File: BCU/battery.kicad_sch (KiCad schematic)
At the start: 5 parts

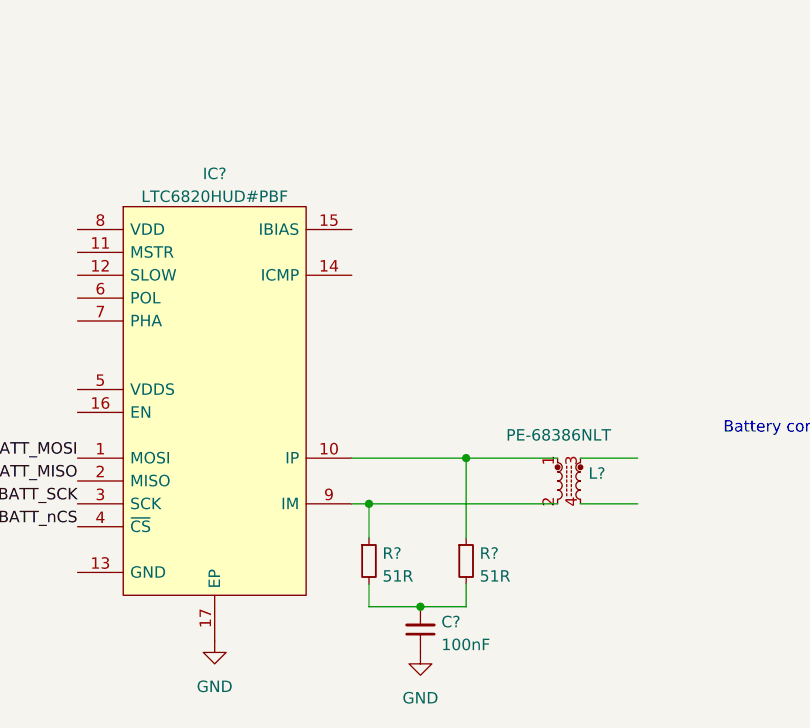
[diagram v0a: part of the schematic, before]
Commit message: Make rough component placement for evaluating missing 3D
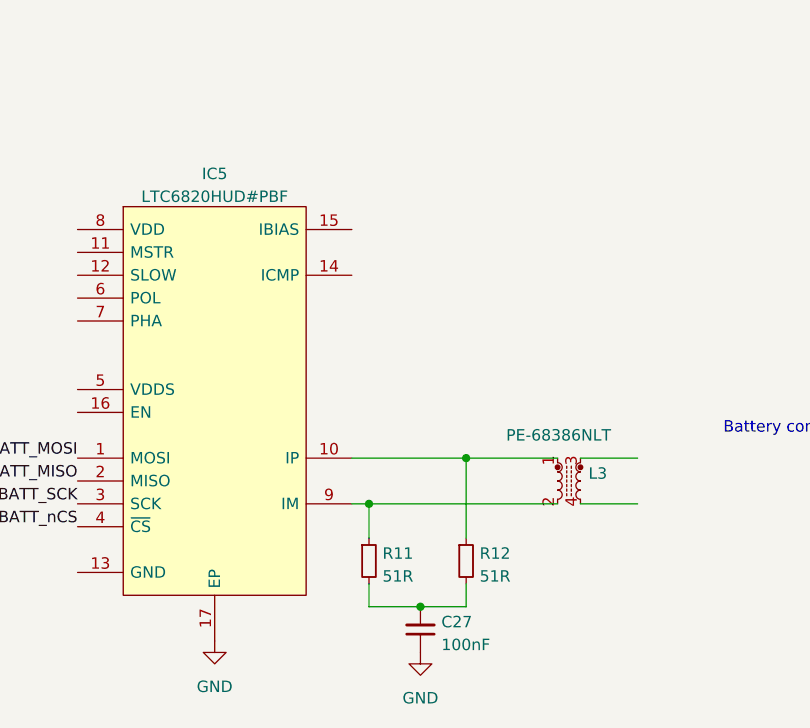
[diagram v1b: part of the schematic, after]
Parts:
- gave numbers to parts that had none: 5
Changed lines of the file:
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@@
   (symbol (lib_id "power:GND") (at 110.49 113.03 0) (unit 1)
     (in_bom yes) (on_board yes) (fields_autoplaced)
-    (property "Reference" "#PWR?" (id 0) (at 110.49 119.38 0)
+    (property "Reference" "#PWR0151" (id 0) (at 110.49 119.38 0)
       (effects (font (size 1.27 1.27)) hide)
     )
@@
   (symbol (lib_id "power:GND") (at 133.35 114.3 0) (unit 1)
     (in_bom yes) (on_board yes) (fields_autoplaced)
-    (property "Reference" "#PWR?" (id 0) (at 133.35 120.65 0)
+    (property "Reference" "#PWR0150" (id 0) (at 133.35 120.65 0)
       (effects (font (size 1.27 1.27)) hide)
     )
@@
   (symbol (lib_id "Device:R_Small") (at 138.43 104.14 0) (unit 1)
     (in_bom yes) (on_board yes) (fields_autoplaced)
-    (property "Reference" "R?" (id 0) (at 139.9286 103.3053 0)
+    (property "Reference" "R12" (id 0) (at 139.9286 103.3053 0)
       (effects (font (size 1.27 1.27)) (justify left))
     )
@@
   (symbol (lib_id "coilchain-com:LTC6820HUD#PBF") (at 110.49 64.77 0) (unit 1)
     (in_bom yes) (on_board yes) (fields_autoplaced)
-    (property "Reference" "IC?" (id 0) (at 110.49 61.121 0))
+    (property "Reference" "IC5" (id 0) (at 110.49 61.121 0))
     (property "Value" "LTC6820HUD#PBF" (id 1) (at 110.49 63.6579 0))
     (property "Footprint" "Package_DFN_QFN:QFN-16-1EP_3x3mm_P0.5mm_EP1.7x1.7mm" (id 2) (at 134.62 67.31 0)
@@
   (symbol (lib_id "Device:C_Small") (at 133.35 111.76 180) (unit 1)
     (in_bom yes) (on_board yes) (fields_autoplaced)
-    (property "Reference" "C?" (id 0) (at 135.6741 110.9189 0)
+    (property "Reference" "C27" (id 0) (at 135.6741 110.9189 0)
       (effects (font (size 1.27 1.27)) (justify right))
     )
@@
   (symbol (lib_id "Device:R_Small") (at 127.635 104.14 0) (unit 1)
     (in_bom yes) (on_board yes) (fields_autoplaced)
-    (property "Reference" "R?" (id 0) (at 129.1336 103.3053 0)
+    (property "Reference" "R11" (id 0) (at 129.1336 103.3053 0)
       (effects (font (size 1.27 1.27)) (justify left))
     )
@@
   (symbol (lib_id "Device:L_Ferrite_Coupled_Small") (at 149.86 95.25 90) (mirror x) (unit 1)
     (in_bom yes) (on_board yes)
-    (property "Reference" "L?" (id 0) (at 152.019 94.4153 90)
+    (property "Reference" "L3" (id 0) (at 152.019 94.4153 90)
       (effects (font (size 1.27 1.27)) (justify right))
     )

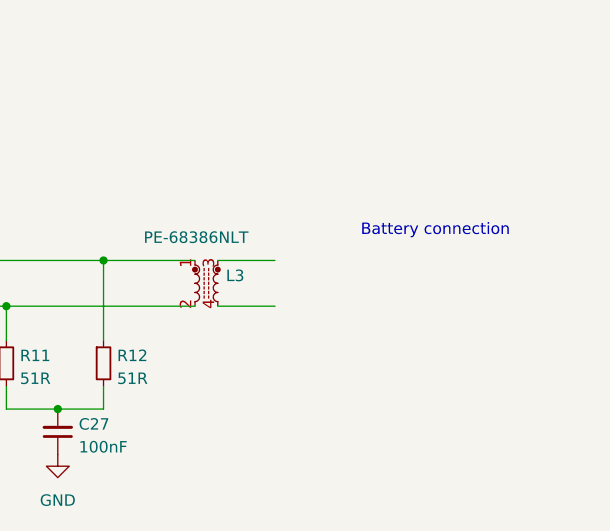
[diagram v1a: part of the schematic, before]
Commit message: change 48v to +BATT, increase cap sizes
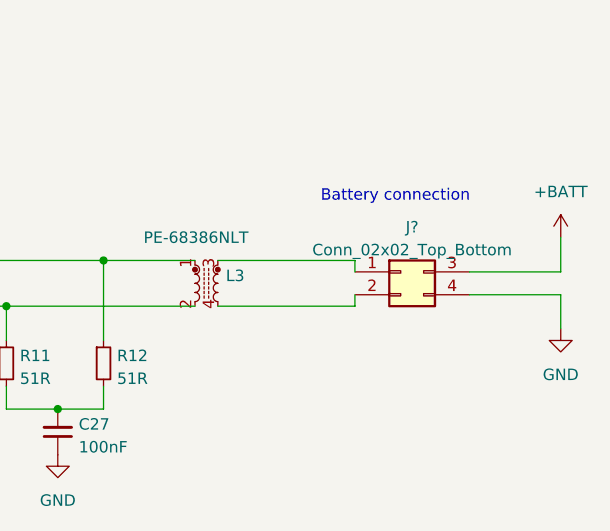
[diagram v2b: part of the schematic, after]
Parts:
- added J?: Conn_02x02_Top_Bottom, symbol Connector_Generic:Conn_02x02_Top_Bottom
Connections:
- net GND: now also J?.4 (Pin_4)
- net at L3.3: now also J?.1 (Pin_1)
- net at L3.4: now also J?.2 (Pin_2)
- new net +BATT: J?.3 (Pin_3)
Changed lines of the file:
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@@
+    (stroke (width 0) (type default) (color 0 0 0 0))
+  )
+  (wire (pts (xy 179.07 96.52) (xy 189.23 96.52))
+    (stroke (width 0) (type default) (color 0 0 0 0))
+  )
+  (wire (pts (xy 189.23 93.98) (xy 189.23 90.17))
     (stroke (width 0) (type default) (color 0 0 0 0))
   )
@@
     (stroke (width 0) (type default) (color 0 0 0 0))
   )
-  (wire (pts (xy 151.13 97.79) (xy 157.48 97.79))
+  (wire (pts (xy 166.37 92.71) (xy 166.37 93.98))
+    (stroke (width 0) (type default) (color 0 0 0 0))
+  )
+  (wire (pts (xy 151.13 97.79) (xy 166.37 97.79))
     (stroke (width 0) (type default) (color 0 0 0 0))
   )
@@
     (stroke (width 0) (type default) (color 0 0 0 0))
   )
+  (wire (pts (xy 179.07 93.98) (xy 189.23 93.98))
+    (stroke (width 0) (type default) (color 0 0 0 0))
+  )
   (wire (pts (xy 127.635 97.79) (xy 127.635 101.6))
     (stroke (width 0) (type default) (color 0 0 0 0))
@@
     (stroke (width 0) (type default) (color 0 0 0 0))
   )
+  (wire (pts (xy 189.23 96.52) (xy 189.23 100.33))
+    (stroke (width 0) (type default) (color 0 0 0 0))
+  )
   (wire (pts (xy 138.43 92.71) (xy 125.73 92.71))
     (stroke (width 0) (type default) (color 0 0 0 0))
@@
     (stroke (width 0) (type default) (color 0 0 0 0))
   )
-  (wire (pts (xy 151.13 92.71) (xy 157.48 92.71))
+  (wire (pts (xy 151.13 92.71) (xy 166.37 92.71))
     (stroke (width 0) (type default) (color 0 0 0 0))
   )
@@
     (stroke (width 0) (type default) (color 0 0 0 0))
   )
+  (wire (pts (xy 166.37 97.79) (xy 166.37 96.52))
+    (stroke (width 0) (type default) (color 0 0 0 0))
+  )
   (wire (pts (xy 36.83 24.13) (xy 46.99 24.13))
     (stroke (width 0) (type default) (color 0 0 0 0))
   )
-  (text "Battery connection" (at 167.005 90.17 0)
+  (text "Battery connection" (at 162.56 86.36 0)
     (effects (font (size 1.27 1.27)) (justify left bottom))
   )
@@
     (effects (font (size 1.27 1.27)) (justify right))
   )
+  (symbol (lib_id "power:+BATT") (at 189.23 90.17 0) (unit 1)
+    (in_bom yes) (on_board yes) (fields_autoplaced)
+    (property "Reference" "#PWR?" (id 0) (at 189.23 93.98 0)
+      (effects (font (size 1.27 1.27)) hide)
+    )
+    (property "Value" "+BATT" (id 1) (at 189.23 85.09 0))
+    (property "Footprint" "" (id 2) (at 189.23 90.17 0)
+      (effects (font (size 1.27 1.27)) hide)
+    )
+    (property "Datasheet" "" (id 3) (at 189.23 90.17 0)
+      (effects (font (size 1.27 1.27)) hide)
+    )
+    (pin "1")
+  )
   (symbol (lib_id "power:GND") (at 110.49 113.03 0) (unit 1)
     (in_bom yes) (on_board yes) (fields_autoplaced)
@@
     )
     (property "Datasheet" "" (id 3) (at 110.49 113.03 0)
+      (effects (font (size 1.27 1.27)) hide)
+    )
+    (pin "1")
+  )
+  (symbol (lib_id "power:GND") (at 189.23 100.33 0) (unit 1)
+    (in_bom yes) (on_board yes) (fields_autoplaced)
+    (property "Reference" "#PWR?" (id 0) (at 189.23 106.68 0)
+      (effects (font (size 1.27 1.27)) hide)
+    )
+    (property "Value" "GND" (id 1) (at 189.23 105.41 0))
+    (property "Footprint" "" (id 2) (at 189.23 100.33 0)
+      (effects (font (size 1.27 1.27)) hide)
+    )
+    (property "Datasheet" "" (id 3) (at 189.23 100.33 0)
       (effects (font (size 1.27 1.27)) hide)
     )
@@
     (pin "2")
   )
+  (symbol (lib_id "Connector_Generic:Conn_02x02_Top_Bottom") (at 171.45 93.98 0) (unit 1)
+    (in_bom yes) (on_board yes) (fields_autoplaced)
+    (property "Reference" "J?" (id 0) (at 172.72 89.0102 0))
+    (property "Value" "Conn_02x02_Top_Bottom" (id 1) (at 172.72 91.5471 0))
+    (property "Footprint" "" (id 2) (at 171.45 93.98 0)
+      (effects (font (size 1.27 1.27)) hide)
+    )
+    (property "Datasheet" "~" (id 3) (at 171.45 93.98 0)
+      (effects (font (size 1.27 1.27)) hide)
+    )
+    (pin "1")
+    (pin "2")
+    (pin "3")
+    (pin "4")
+  )
   (symbol (lib_id "Device:R_Small") (at 127.635 104.14 0) (unit 1)

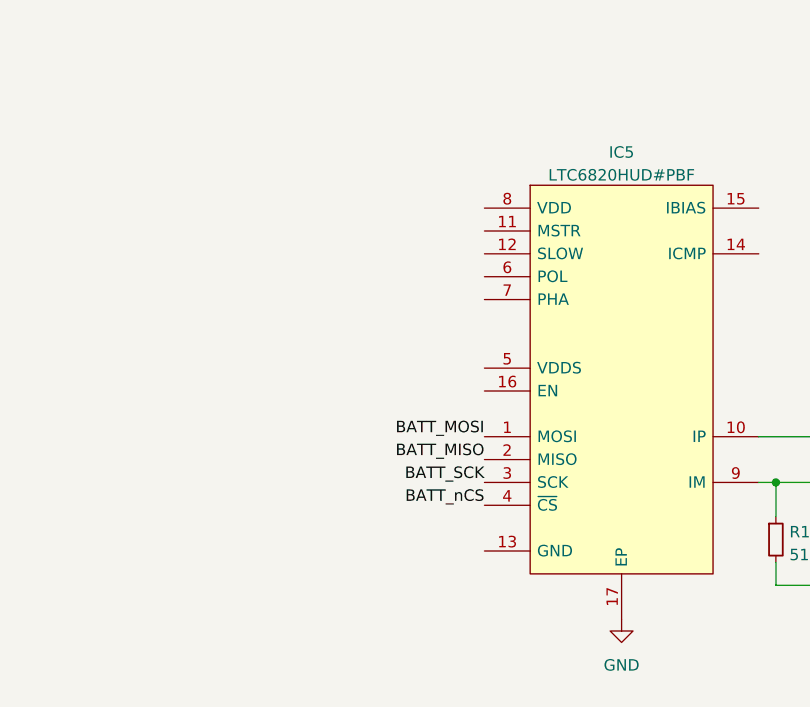
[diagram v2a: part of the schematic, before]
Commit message: Added power enable logic
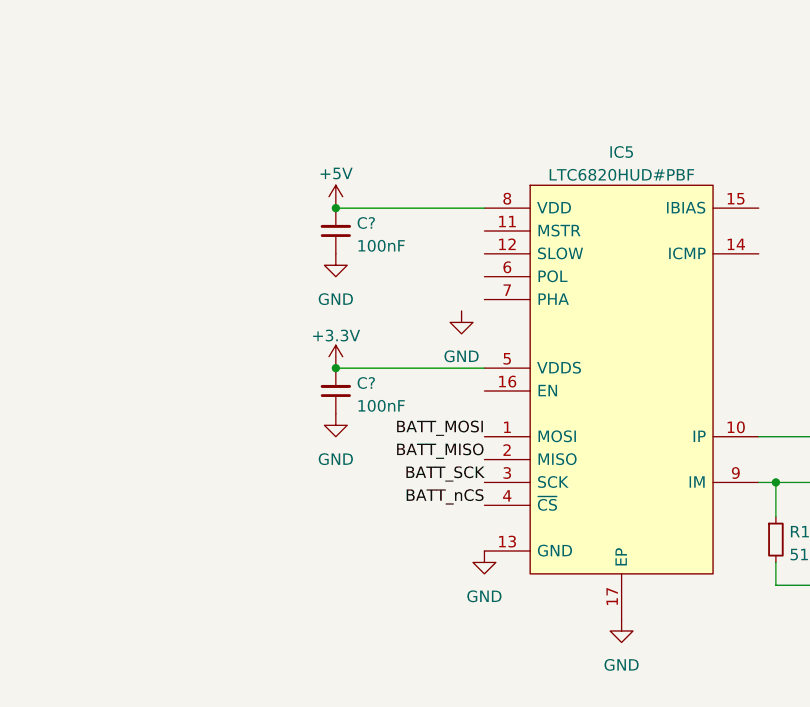
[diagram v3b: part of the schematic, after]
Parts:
- added C? (x2): 100nF, Capacitor_SMD:C_0402_1005Metric_Pad0.74x0.62mm_HandSolder, symbol Device:C_Small
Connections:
- net GND: now also IC5.13 (GND), C?.1, C?.1
- net +3V3: now reaches IC5.5 (VDDS)
- net +3V3: now also C?.2
- net +5V: now reaches IC5.8 (VDD)
- net +5V: now also C?.2
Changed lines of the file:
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@@
   (junction (at 127.635 97.79) (diameter 0) (color 0 0 0 0)
   )
+  (junction (at 78.74 67.31) (diameter 0) (color 0 0 0 0)
+  )
   (junction (at 133.35 109.22) (diameter 0) (color 0 0 0 0)
   )
   (junction (at 138.43 92.71) (diameter 0) (color 0 0 0 0)
   )
+  (junction (at 78.74 85.09) (diameter 0) (color 0 0 0 0)
+  )
   (bus_entry (at 34.29 21.59) (size 2.54 2.54)
     (stroke (width 0) (type default) (color 0 0 0 0))
@@
     (stroke (width 0) (type default) (color 0 0 0 0))
   )
+  (wire (pts (xy 78.74 85.09) (xy 95.25 85.09))
+    (stroke (width 0) (type default) (color 0 0 0 0))
+  )
   (wire (pts (xy 127.635 97.79) (xy 148.59 97.79))
     (stroke (width 0) (type default) (color 0 0 0 0))
@@
   )
   (wire (pts (xy 138.43 109.22) (xy 133.35 109.22))
+    (stroke (width 0) (type default) (color 0 0 0 0))
+  )
+  (wire (pts (xy 78.74 67.31) (xy 95.25 67.31))
     (stroke (width 0) (type default) (color 0 0 0 0))
   )
@@
     (effects (font (size 1.27 1.27)) (justify right))
   )
+  (symbol (lib_id "power:GND") (at 78.74 90.17 0) (unit 1)
+    (in_bom yes) (on_board yes) (fields_autoplaced)
+    (property "Reference" "#PWR?" (id 0) (at 78.74 96.52 0)
+      (effects (font (size 1.27 1.27)) hide)
+    )
+    (property "Value" "GND" (id 1) (at 78.74 95.25 0))
+    (property "Footprint" "" (id 2) (at 78.74 90.17 0)
+      (effects (font (size 1.27 1.27)) hide)
+    )
+    (property "Datasheet" "" (id 3) (at 78.74 90.17 0)
+      (effects (font (size 1.27 1.27)) hide)
+    )
+    (pin "1")
+  )
   (symbol (lib_id "power:+BATT") (at 189.23 90.17 0) (unit 1)
     (in_bom yes) (on_board yes) (fields_autoplaced)
@@
     (pin "1")
   )
+  (symbol (lib_id "Device:C_Small") (at 78.74 69.85 180) (unit 1)
+    (in_bom yes) (on_board yes) (fields_autoplaced)
+    (property "Reference" "C?" (id 0) (at 81.0641 69.0089 0)
+      (effects (font (size 1.27 1.27)) (justify right))
+    )
+    (property "Value" "100nF" (id 1) (at 81.0641 71.5458 0)
+      (effects (font (size 1.27 1.27)) (justify right))
+    )
+    (property "Footprint" "Capacitor_SMD:C_0402_1005Metric_Pad0.74x0.62mm_HandSolder" (id 2) (at 78.74 69.85 0)
+      (effects (font (size 1.27 1.27)) hide)
+    )
+    (property "Datasheet" "~" (id 3) (at 78.74 69.85 0)
+      (effects (font (size 1.27 1.27)) hide)
+    )
+    (pin "1")
+    (pin "2")
+  )
   (symbol (lib_id "power:GND") (at 133.35 114.3 0) (unit 1)
     (in_bom yes) (on_board yes) (fields_autoplaced)
@@
     (pin "1")
   )
+  (symbol (lib_id "Device:C_Small") (at 78.74 87.63 180) (unit 1)
+    (in_bom yes) (on_board yes) (fields_autoplaced)
+    (property "Reference" "C?" (id 0) (at 81.0641 86.7889 0)
+      (effects (font (size 1.27 1.27)) (justify right))
+    )
+    (property "Value" "100nF" (id 1) (at 81.0641 89.3258 0)
+      (effects (font (size 1.27 1.27)) (justify right))
+    )
+    (property "Footprint" "Capacitor_SMD:C_0402_1005Metric_Pad0.74x0.62mm_HandSolder" (id 2) (at 78.74 87.63 0)
+      (effects (font (size 1.27 1.27)) hide)
+    )
+    (property "Datasheet" "~" (id 3) (at 78.74 87.63 0)
+      (effects (font (size 1.27 1.27)) hide)
+    )
+    (pin "1")
+    (pin "2")
+  )
+  (symbol (lib_id "power:+5V") (at 78.74 67.31 0) (unit 1)
+    (in_bom yes) (on_board yes)
+    (property "Reference" "#PWR?" (id 0) (at 78.74 71.12 0)
+      (effects (font (size 1.27 1.27)) hide)
+    )
+    (property "Value" "+5V" (id 1) (at 78.74 63.5 0))
+    (property "Footprint" "" (id 2) (at 78.74 67.31 0)
+      (effects (font (size 1.27 1.27)) hide)
+    )
+    (property "Datasheet" "" (id 3) (at 78.74 67.31 0)
+      (effects (font (size 1.27 1.27)) hide)
+    )
+    (pin "1")
+  )
   (symbol (lib_id "Device:R_Small") (at 138.43 104.14 0) (unit 1)
     (in_bom yes) (on_board yes) (fields_autoplaced)
@@
     (pin "1")
     (pin "2")
+  )
+  (symbol (lib_id "power:+3.3V") (at 78.74 85.09 0) (unit 1)
+    (in_bom yes) (on_board yes) (fields_autoplaced)
+    (property "Reference" "#PWR?" (id 0) (at 78.74 88.9 0)
+      (effects (font (size 1.27 1.27)) hide)
+    )
+    (property "Value" "+3.3V" (id 1) (at 78.74 81.5142 0))
+    (property "Footprint" "" (id 2) (at 78.74 85.09 0)
+      (effects (font (size 1.27 1.27)) hide)
+    )
+    (property "Datasheet" "" (id 3) (at 78.74 85.09 0)
+      (effects (font (size 1.27 1.27)) hide)
+    )
+    (pin "1")
   )
   (symbol (lib_id "coilchain-com:LTC6820HUD#PBF") (at 110.49 64.77 0) (unit 1)
@@
     (pin "9")
   )
+  (symbol (lib_id "power:GND") (at 95.25 105.41 0) (unit 1)
+    (in_bom yes) (on_board yes) (fields_autoplaced)
+    (property "Reference" "#PWR?" (id 0) (at 95.25 111.76 0)
+      (effects (font (size 1.27 1.27)) hide)
+    )
+    (property "Value" "GND" (id 1) (at 95.25 110.49 0))
+    (property "Footprint" "" (id 2) (at 95.25 105.41 0)
+      (effects (font (size 1.27 1.27)) hide)
+    )
+    (property "Datasheet" "" (id 3) (at 95.25 105.41 0)
+      (effects (font (size 1.27 1.27)) hide)
+    )
+    (pin "1")
+  )
+  (symbol (lib_id "power:GND") (at 78.74 72.39 0) (unit 1)
+    (in_bom yes) (on_board yes) (fields_autoplaced)
+    (property "Reference" "#PWR?" (id 0) (at 78.74 78.74 0)
+      (effects (font (size 1.27 1.27)) hide)
+    )
+    (property "Value" "GND" (id 1) (at 78.74 77.47 0))
+    (property "Footprint" "" (id 2) (at 78.74 72.39 0)
+      (effects (font (size 1.27 1.27)) hide)
+    )
+    (property "Datasheet" "" (id 3) (at 78.74 72.39 0)
+      (effects (font (size 1.27 1.27)) hide)
+    )
+    (pin "1")
+  )
+  (symbol (lib_id "power:GND") (at 92.71 78.74 0) (unit 1)
+    (in_bom yes) (on_board yes) (fields_autoplaced)
+    (property "Reference" "#PWR?" (id 0) (at 92.71 85.09 0)
+      (effects (font (size 1.27 1.27)) hide)
+    )
+    (property "Value" "GND" (id 1) (at 92.71 83.82 0))
+    (property "Footprint" "" (id 2) (at 92.71 78.74 0)
+      (effects (font (size 1.27 1.27)) hide)
+    )
+    (property "Datasheet" "" (id 3) (at 92.71 78.74 0)
+      (effects (font (size 1.27 1.27)) hide)
+    )
+    (pin "1")
+  )
   (symbol (lib_id "Device:C_Small") (at 133.35 111.76 180) (unit 1)
